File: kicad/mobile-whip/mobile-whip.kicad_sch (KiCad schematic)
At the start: 51 parts, among them J1 SMA Edge Mount Male, J2 USB_C_Receptacle_USB2.0, Q1 SI2301CDS-T1-GE3, Q2 SI2301CDS-T1-GE3, SW1 MK-12C02-G025, U1 LTC6268IS6, U2 TP4054, U3 LP2985-3.3, U4 TLV431

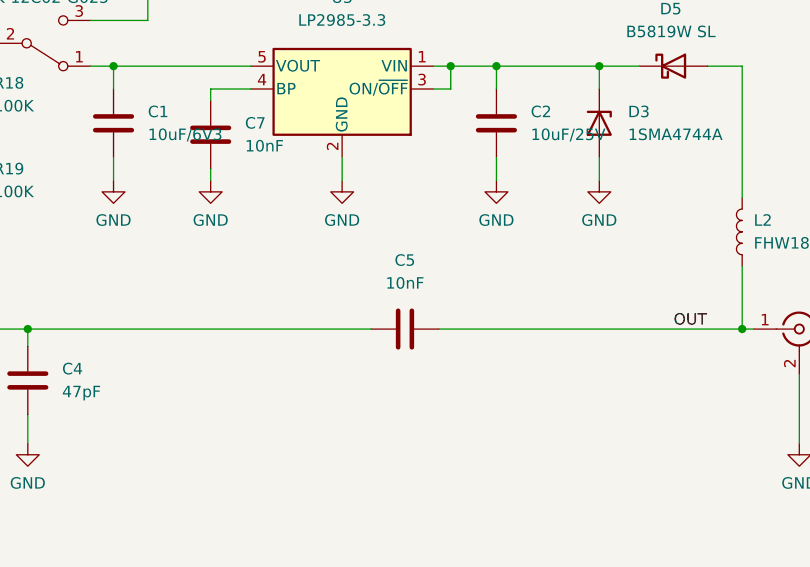
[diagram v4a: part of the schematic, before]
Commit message: Use 100nF AC coupling cap
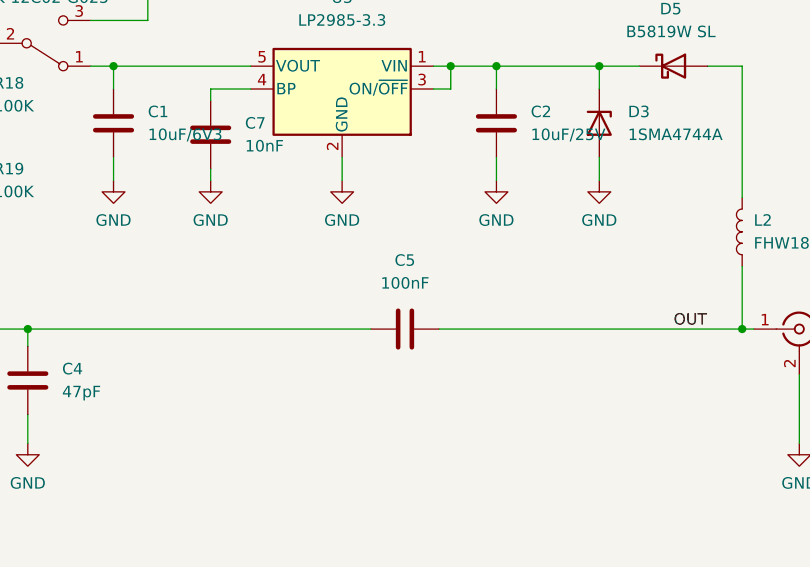
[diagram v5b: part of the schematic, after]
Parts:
- C5: value 10nF -> 100nF
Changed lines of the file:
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@@
     (in_bom yes) (on_board yes) (fields_autoplaced)
     (property "Reference" "C5" (id 0) (at 168.91 104.14 90))
-    (property "Value" "10nF" (id 1) (at 168.91 106.68 90))
+    (property "Value" "100nF" (id 1) (at 168.91 106.68 90))
     (property "Footprint" "Capacitor_SMD:C_0805_2012Metric" (id 2) (at 172.72 110.7948 0)
       (effects (font (size 1.27 1.27)) hide)
@@
     )
     (path "/3c5248a3-8f3f-476f-a470-b075e2a60306"
-      (reference "C5") (unit 1) (value "10nF") (footprint "Capacitor_SMD:C_0805_2012Metric")
+      (reference "C5") (unit 1) (value "100nF") (footprint "Capacitor_SMD:C_0805_2012Metric")
     )
     (path "/2dbfcc83-037d-45d3-a843-f93d44828d77"

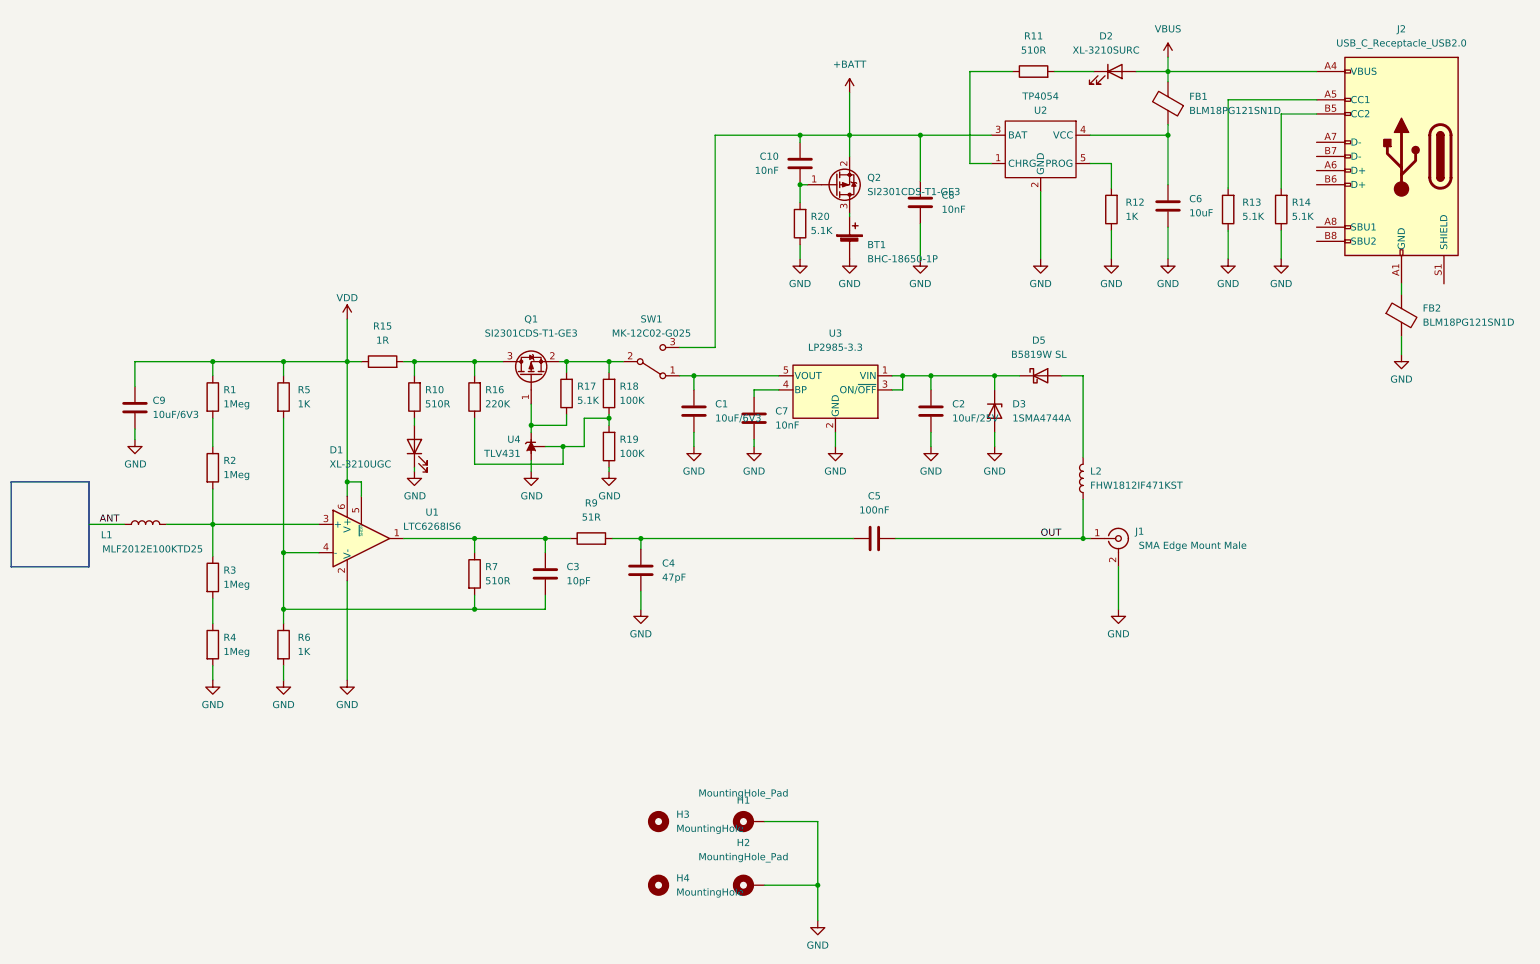
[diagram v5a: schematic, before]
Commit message: Changed some resistor values
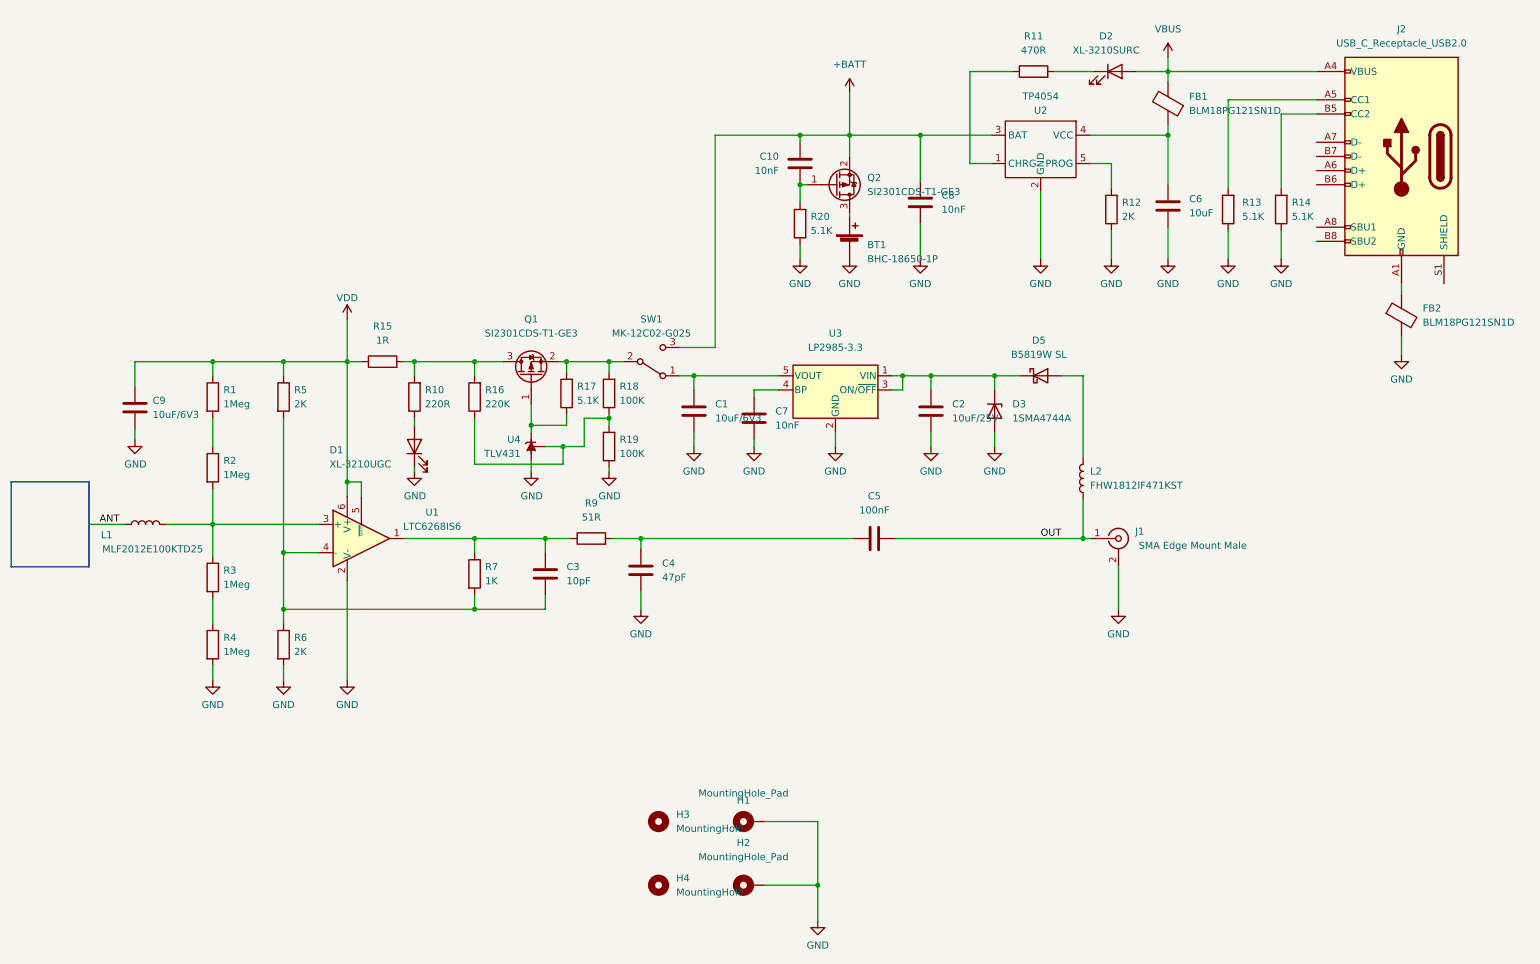
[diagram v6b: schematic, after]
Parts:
- R10: value 510R -> 220R
- R11: value 510R -> 470R
- R12, R5, R6: value 1K -> 2K
- R7: value 510R -> 1K
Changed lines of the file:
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@@
   (symbol (lib_id "Device:R") (at 62.865 86.36 0) (unit 1)
     (in_bom yes) (on_board yes) (fields_autoplaced)
-    (property "Reference" "R5" (id 0) (at 65.405 85.0899 0)
-      (effects (font (size 1.27 1.27)) (justify left))
-    )
-    (property "Value" "1K" (id 1) (at 65.405 87.6299 0)
+    (property "Reference" "R5" (id 0) (at 64.77 85.0899 0)
+      (effects (font (size 1.27 1.27)) (justify left))
+    )
+    (property "Value" "2K" (id 1) (at 64.77 87.6299 0)
       (effects (font (size 1.27 1.27)) (justify left))
     )
@@
       (effects (font (size 1.27 1.27)) (justify right))
     )
-    (property "Value" "510R" (id 1) (at 88.265 87.6299 0)
+    (property "Value" "220R" (id 1) (at 88.265 87.6299 0)
       (effects (font (size 1.27 1.27)) (justify right))
     )
@@
   (symbol (lib_id "Device:R") (at 211.455 52.705 180) (unit 1)
     (in_bom yes) (on_board yes) (fields_autoplaced)
-    (property "Reference" "R12" (id 0) (at 213.995 51.4349 0)
-      (effects (font (size 1.27 1.27)) (justify right))
-    )
-    (property "Value" "1K" (id 1) (at 213.995 53.9749 0)
+    (property "Reference" "R12" (id 0) (at 213.36 51.4349 0)
+      (effects (font (size 1.27 1.27)) (justify right))
+    )
+    (property "Value" "2K" (id 1) (at 213.36 53.9749 0)
       (effects (font (size 1.27 1.27)) (justify right))
     )
@@
       (effects (font (size 1.27 1.27)) (justify left))
     )
-    (property "Value" "510R" (id 1) (at 99.06 119.3799 0)
+    (property "Value" "1K" (id 1) (at 99.06 119.3799 0)
       (effects (font (size 1.27 1.27)) (justify left))
     )
@@
   (symbol (lib_id "Device:R") (at 62.865 130.81 0) (unit 1)
     (in_bom yes) (on_board yes) (fields_autoplaced)
-    (property "Reference" "R6" (id 0) (at 65.405 129.5399 0)
-      (effects (font (size 1.27 1.27)) (justify left))
-    )
-    (property "Value" "1K" (id 1) (at 65.405 132.0799 0)
+    (property "Reference" "R6" (id 0) (at 64.77 129.5399 0)
+      (effects (font (size 1.27 1.27)) (justify left))
+    )
+    (property "Value" "2K" (id 1) (at 64.77 132.0799 0)
       (effects (font (size 1.27 1.27)) (justify left))
     )
@@
     (in_bom yes) (on_board yes) (fields_autoplaced)
     (property "Reference" "R11" (id 0) (at 197.485 21.59 90))
-    (property "Value" "510R" (id 1) (at 197.485 24.13 90))
+    (property "Value" "470R" (id 1) (at 197.485 24.13 90))
     (property "Footprint" "Resistor_SMD:R_0805_2012Metric" (id 2) (at 197.485 29.718 90)
       (effects (font (size 1.27 1.27)) hide)
@@
     )
     (path "/1878959e-e5a0-4826-844b-8f80ab886b5a"
-      (reference "R5") (unit 1) (value "1K") (footprint "Resistor_SMD:R_0805_2012Metric")
+      (reference "R5") (unit 1) (value "2K") (footprint "Resistor_SMD:R_0805_2012Metric")
     )
     (path "/83815bd5-67b6-4b95-840e-a349881c1d3a"
-      (reference "R6") (unit 1) (value "1K") (footprint "Resistor_SMD:R_0805_2012Metric")
+      (reference "R6") (unit 1) (value "2K") (footprint "Resistor_SMD:R_0805_2012Metric")
     )
     (path "/7df6fdfa-b2b9-456c-9463-7925942a69e5"
-      (reference "R7") (unit 1) (value "510R") (footprint "Resistor_SMD:R_0805_2012Metric")
+      (reference "R7") (unit 1) (value "1K") (footprint "Resistor_SMD:R_0805_2012Metric")
     )
     (path "/a493556d-5c89-4b22-8fa7-8d9eb52a51f3"
@@
     )
     (path "/21334618-8ea5-486c-b9b5-5dfbd4e69037"
-      (reference "R10") (unit 1) (value "510R") (footprint "Resistor_SMD:R_0805_2012Metric")
+      (reference "R10") (unit 1) (value "220R") (footprint "Resistor_SMD:R_0805_2012Metric")
     )
     (path "/af38408d-7ade-4298-bd81-67285680b2ca"
-      (reference "R11") (unit 1) (value "510R") (footprint "Resistor_SMD:R_0805_2012Metric")
+      (reference "R11") (unit 1) (value "470R") (footprint "Resistor_SMD:R_0805_2012Metric")
     )
     (path "/4d6d76aa-61d4-45af-81b5-c851915ddf93"
-      (reference "R12") (unit 1) (value "1K") (footprint "Resistor_SMD:R_0805_2012Metric")
+      (reference "R12") (unit 1) (value "2K") (footprint "Resistor_SMD:R_0805_2012Metric")
     )
     (path "/c949f6d5-cbde-45aa-8c97-61d997f776a3"

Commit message: Final touches
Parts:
- added C11: 100nF, Capacitor_SMD:C_0805_2012Metric, symbol Device:C
- added D4, D6: B5819W SL, Diode_SMD:D_SOD-123, symbol Device:D_Schottky
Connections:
- net GND: now also C11.1, D6.2 (A)
- net VDD: now also Q1.3 (D), R10.2, R15.2, R16.2, C11.2, D4.1 (K); no longer C9.1, R1.1, R15.1, R5.1, U1.5 (~{SHDN}), U1.6 (V+)
- net at C4.1, C5.1, R9.2: now also D4.2 (A), D6.1 (K)
- new net: C9.1, R1.1, R15.1, R5.1, U1.5 (~{SHDN}), U1.6 (V+)

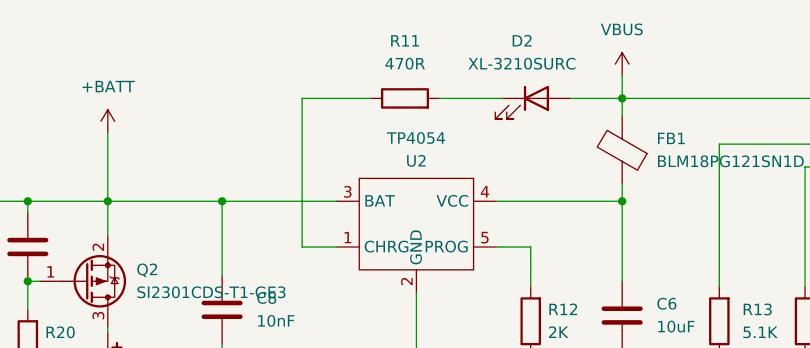
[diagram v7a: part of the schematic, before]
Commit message: Adjust lithium cell footprint and change red LED resistor to 220R
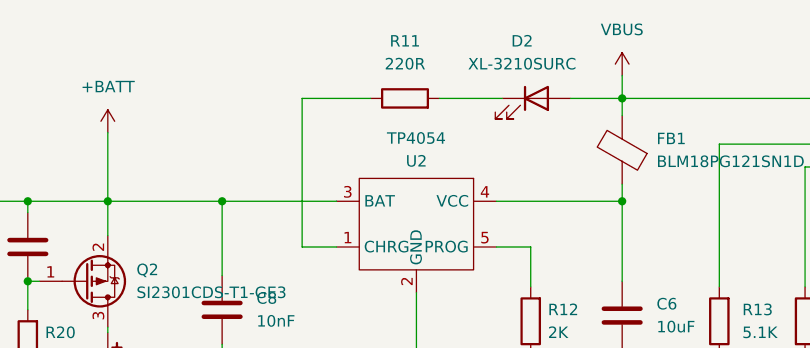
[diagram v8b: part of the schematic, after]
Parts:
- R11: value 470R -> 220R
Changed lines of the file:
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@@
     (in_bom yes) (on_board yes) (fields_autoplaced)
     (property "Reference" "R11" (id 0) (at 197.485 21.59 90))
-    (property "Value" "470R" (id 1) (at 197.485 24.13 90))
+    (property "Value" "220R" (id 1) (at 197.485 24.13 90))
     (property "Footprint" "Resistor_SMD:R_0805_2012Metric" (id 2) (at 197.485 29.718 90)
       (effects (font (size 1.27 1.27)) hide)
@@
     )
     (path "/af38408d-7ade-4298-bd81-67285680b2ca"
-      (reference "R11") (unit 1) (value "470R") (footprint "Resistor_SMD:R_0805_2012Metric")
+      (reference "R11") (unit 1) (value "220R") (footprint "Resistor_SMD:R_0805_2012Metric")
     )
     (path "/4d6d76aa-61d4-45af-81b5-c851915ddf93"
